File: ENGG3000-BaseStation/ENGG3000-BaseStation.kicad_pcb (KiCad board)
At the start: 4 copper layers, 29 parts, among them J1 Board Power, J2 OLED, J4 USB_C_Receptacle_USB2.0_16P, Q1 SS8050, SW1 RESET, SW2 BOOT, U1 ESP32-S3-WROOM-1-N16R8, U5 AMS1117-3.3

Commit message: Schematic update
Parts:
- removed U5: AMS1117-3.3, Package_TO_SOT_SMD:SOT-223-3_TabPin2
- removed UART0: UART0, Connector_JST:JST_XH_B4B-XH-A_1x04_P2.50mm_Vertical
- added C5: 100nF, Capacitor_SMD:C_0402_1005Metric, F.Cu at (148.8, 74.9)
- added C6: 10uF, Capacitor_Tantalum_SMD:CP_EIA-3216-18_Kemet-A, F.Cu at (149.1, 79.8)
- added C7: 10uF, Capacitor_Tantalum_SMD:CP_EIA-3216-18_Kemet-A, F.Cu at (149.1, 82.9)
- added C8: 1uF, Capacitor_SMD:C_0402_1005Metric, F.Cu at (148.8, 76.8)
- added D4: 5V, LED_SMD:LED_0603_1608Metric, F.Cu at (149.1, 101.7)
- added D5: 3.3V, LED_SMD:LED_0805_2012Metric, F.Cu at (118.7, 102.3)
- added D6: STATUS, LED_SMD:LED_0805_2012Metric, F.Cu at (118.7, 105.3)
- added J3: Cell 1, Connector_JST:JST_XH_B2B-XH-A_1x02_P2.50mm_Vertical, F.Cu at (115.0, 85.0)
- added J5: OLED, Connector_PinHeader_2.54mm:PinHeader_1x04_P2.54mm_Vertical, F.Cu at (123.2, 68.3)
- added J6: Buttons, Connector_PinHeader_2.54mm:PinHeader_1x05_P2.54mm_Vertical, F.Cu at (144.8, 90.6)
- added J7: USB_C_Receptacle_USB2.0_16P, Connector_USB:USB_C_Receptacle_G-Switch_GT-USB-7010ASV, F.Cu at (140.3, 83.6)
- added J8: UltrasonicA, Connector_PinHeader_2.54mm:PinHeader_1x04_P2.54mm_Vertical, F.Cu at (127.8, 68.3)
- added J9: UltrasonicB, Connector_PinHeader_2.54mm:PinHeader_1x04_P2.54mm_Vertical, F.Cu at (132.4, 68.3)
- added L1: 2.2uH, Inductor_SMD:L_APV_ANR4020, F.Cu at (137.3, 103.8)
- added Q2: SS8050, Package_TO_SOT_SMD:SOT-23, F.Cu at (114.0, 104.4)
- added R13: 10k, Resistor_SMD:R_0402_1005Metric, F.Cu at (128.2, 92.8)
- added R14: 1k, Resistor_SMD:R_0402_1005Metric, F.Cu at (128.2, 94.7)
- added R15: 10k, Resistor_SMD:R_0402_1005Metric, F.Cu at (128.2, 96.7)
- added R16: 22, Resistor_SMD:R_0402_1005Metric, F.Cu at (128.2, 98.7)
- added R17: 100R, Resistor_SMD:R_0402_1005Metric, F.Cu at (128.2, 100.7)
- added R18: 1k, Resistor_SMD:R_0402_1005Metric, F.Cu at (128.2, 102.7)
- added R19: 5.1k, Resistor_SMD:R_0402_1005Metric, F.Cu at (131.1, 92.8)
- added R21: 5.1k, Resistor_SMD:R_0402_1005Metric, F.Cu at (131.1, 96.7)
- added R22: 5.1k, Resistor_SMD:R_0402_1005Metric, F.Cu at (131.1, 98.7)
- added R23: 5.1k, Resistor_SMD:R_0402_1005Metric, F.Cu at (131.1, 100.7)
- added R9: 5.1k, Resistor_SMD:R_0402_1005Metric, F.Cu at (125.3, 96.7)
- added U3: TPS63001DRCR, Package_SON:Texas_DRC0010J_ThermalVias, F.Cu at (149.6, 97.9)
- added UART1: UART0, Connector_PinHeader_2.54mm:PinHeader_1x04_P2.54mm_Vertical, F.Cu at (137.0, 68.3)
- C1: value 10uF -> 1uF
- C2: value 10uF -> 1uF; footprint Capacitor_Tantalum_SMD:CP_EIA-3216-18_Kemet-A -> Capacitor_SMD:C_0402_1005Metric
- C3: value 1uF -> 10uF
- C4: footprint Capacitor_Tantalum_SMD:CP_EIA-3216-18_Kemet-A -> Capacitor_SMD:C_0402_1005Metric
- D1: value 5V -> CHRG; footprint LED_SMD:LED_0603_1608Metric -> LED_SMD:LED_0805_2012Metric
- D2: value 3.3V -> SS14; footprint LED_SMD:LED_0805_2012Metric -> Diode_SMD:D_SMA
- D3: value L -> SS14; footprint LED_SMD:LED_0805_2012Metric -> Diode_SMD:D_SMA
- J1: value Board Power -> CHRG LED; footprint Connector_JST:JST_XH_B3B-XH-A_1x03_P2.50mm_Vertical -> Connector_JST:JST_XH_B2B-XH-A_1x02_P2.50mm_Vertical
- J2: value OLED -> Cell 2; footprint Connector_JST:JST_XH_B4B-XH-A_1x04_P2.50mm_Vertical -> Connector_JST:JST_XH_B2B-XH-A_1x02_P2.50mm_Vertical
- J4: value USB_C_Receptacle_USB2.0_16P -> Power Switch; footprint Connector_USB:USB_C_Receptacle_G-Switch_GT-USB-7010ASV -> Connector_PinHeader_2.54mm:PinHeader_1x02_P2.54mm_Vertical
- Q1: value SS8050 -> AO3401A
- R1: value 5.1k -> 1k
- R12: value 10k -> 22
- R2: value 5.1k -> 1.5k
- R20: value 1k -> 5.1k
- R3: value 22 -> 5.1k
- R4: value 22 -> 51k
- R5: value 5.1k -> 200k
- R6, R7: value 5.1k -> 10k
- U1: value ESP32-S3-WROOM-1-N16R8 -> CN3085; footprint PCM_Espressif:ESP32-S3-WROOM-1 -> JLCPCB_Power_Management_ICs:SOP-8_L4.9-W3.9-P1.27-LS6.0-BL-EP
- moved C1 45.0 mm to (148.8, 67.0)
- moved C3 43.2 mm to (148.8, 70.9)
- moved J1 38.6 mm to (115.0, 69.4)
- moved D1 38.2 mm to (118.7, 99.3)
- moved D2 32.3 mm to (143.4, 68.3)
- moved D3 30.9 mm to (143.4, 72.8)
- moved R7 30.0 mm to (125.3, 92.8)
- moved R8 30.0 mm to (125.3, 94.7)
- moved R10 29.3 mm to (125.3, 98.7)
- moved R12 29.3 mm to (125.3, 102.7)
- moved R11 29.3 mm to (125.3, 100.7)
- moved R5 29.0 mm to (122.4, 100.7)
- moved R6 29.0 mm to (122.4, 102.7)
- moved SW1 28.4 mm to (138.5, 91.5)
- moved R1 28.2 mm to (122.4, 92.8)
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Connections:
- C1 pad 1: GND -> +5V
- C1 pad 2: +5V -> GND
- C2 pad 1: +3.3V -> Net-(U2-EN)
- C3 pad 1: Net-(U1-EN) -> BAT
- C4 pad 1: +3.3V -> Net-(U1-RC)
- D1 pad 1: GND -> Net-(D1-K)
- D2 pad 1: GND -> Net-(D2-K)
- D2 pad 2: Net-(D2-A) -> BAT
- D3 pad 1: GND -> Net-(D3-K)
- D3 pad 2: Net-(D3-A) -> +5V
- J1 pad 1: GND -> Net-(D1-K)
- J1 pad 2: +3.3V -> Net-(J1-VCC)
- J2 pad 1: GND -> Net-(J2--)
- J2 pad 2: SDA -> BAT
- Q1 pad 1: Net-(Q1-B) -> Net-(Q1-G)
- Q1 pad 2: GND -> Net-(D2-K)
- Q1 pad 3: Net-(BZ1--) -> Net-(D3-K)
- R1 pad 1: GND -> Net-(U1-ISET)
- R1 pad 2: Net-(J4-CC2) -> Net-(R1-Pad2)
- R10 pad 1: Net-(U1-GPIO0/BOOT) -> Net-(U2-GPIO0/BOOT)
- R11 pad 1: SDA -> GND
- R11 pad 2: +3.3V -> Net-(Q1-G)
- R12 pad 1: SCL -> /ESP_D+
- R12 pad 2: +3.3V -> D+
- R2 pad 1: GND -> Net-(R1-Pad2)
- R2 pad 2: Net-(J4-CC1) -> GND
- R20 pad 1: GPIO41 -> GND
- R20 pad 2: Net-(Q1-B) -> Net-(J7-CC2)
- R3 pad 1: /ESP_D+ -> +3.3V
- R3 pad 2: /D+ -> Net-(U2-EN)
- R4 pad 1: /ESP_D- -> +5V
- R4 pad 2: /D- -> Net-(R4-Pad2)
- R5 pad 1: +5V -> Net-(R4-Pad2)
- R5 pad 2: Net-(D1-A) -> Net-(U1-RC)
- R6 pad 1: +3.3V -> BAT
- R6 pad 2: Net-(D2-A) -> FB
- R7 pad 1: GPIO40 -> FB
- R7 pad 2: Net-(D3-A) -> GND
- R8 pad 1: +3.3V -> Net-(J1-VCC)
- R8 pad 2: Net-(U1-EN) -> +5V
- SW1 pad 2: Net-(U1-EN) -> Net-(U2-EN)
- SW2 pad 1: Net-(U1-GPIO0/BOOT) -> Net-(U2-GPIO0/BOOT)
- U1 pad 2: +3.3V -> Net-(U1-ISET)
- U1 pad 3: Net-(U1-EN) -> GND
- U1 pad 4: unconnected-(U1-GPIO4/TOUCH4/ADC1_CH3-Pad4) -> +5V
- U1 pad 5: unconnected-(U1-GPIO5/TOUCH5/ADC1_CH4-Pad5) -> BAT
- U1 pad 6: unconnected-(U1-GPIO6/TOUCH6/ADC1_CH5-Pad6) -> Net-(U1-RC)
- U1 pad 7: unconnected-(U1-GPIO7/TOUCH7/ADC1_CH6-Pad7) -> Net-(D1-K)
- U1 pad 8: unconnected-(U1-GPIO15/U0RTS/ADC2_CH4/XTAL_32K_P-Pad8) -> FB
- U1 pad 9: unconnected-(U1-GPIO16/U0CTS/ADC2_CH5/XTAL_32K_N-Pad9) -> GND

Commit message: Kicad footprint update
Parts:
- removed D6: STATUS, LED_SMD:LED_0805_2012Metric
- removed J6: Buttons, Connector_PinHeader_2.54mm:PinHeader_1x05_P2.54mm_Vertical
- removed R16: 22, Resistor_SMD:R_0402_1005Metric
- added C9: 10uF, Capacitor_SMD:C_0805_2012Metric, F.Cu at (125.2, 70.4)
- added J10: Cell/Pack 1, Connector_JST:JST_XH_B2B-XH-A_1x02_P2.50mm_Vertical, F.Cu at (114.7, 92.6)
- added JP1: SolderJumper, Jumper:SolderJumper-2_P1.3mm_Bridged2Bar_RoundedPad1.0x1.5mm, F.Cu at (122.4, 81.5)
- added JP2: SolderJumper, Jumper:SolderJumper-2_P1.3mm_Bridged2Bar_RoundedPad1.0x1.5mm, F.Cu at (122.4, 89.0)
- added U2: TPS63001DRCR, Package_SON:Texas_DRC0010J_ThermalVias, F.Cu at (132.9, 91.9)
- C2: value 1uF -> 10uF; footprint Capacitor_SMD:C_0402_1005Metric -> Capacitor_Tantalum_SMD:CP_EIA-3216-18_Kemet-A
- C3: footprint Capacitor_SMD:C_0402_1005Metric -> Capacitor_Tantalum_SMD:CP_EIA-3216-18_Kemet-A
- C4: value 10uF -> 1uF
- C5: value 100nF -> 10uF; footprint Capacitor_SMD:C_0402_1005Metric -> Capacitor_SMD:C_0805_2012Metric
- C6: value 10uF -> 100nF; footprint Capacitor_Tantalum_SMD:CP_EIA-3216-18_Kemet-A -> Capacitor_SMD:C_0402_1005Metric
- C7: value 10uF -> 1uF; footprint Capacitor_Tantalum_SMD:CP_EIA-3216-18_Kemet-A -> Capacitor_SMD:C_0402_1005Metric
- C8: value 1uF -> 10uF; footprint Capacitor_SMD:C_0402_1005Metric -> Capacitor_SMD:C_0805_2012Metric
- D1: value CHRG -> 5V; footprint LED_SMD:LED_0805_2012Metric -> LED_SMD:LED_0603_1608Metric
- D2: value SS14 -> 3.3V; footprint Diode_SMD:D_SMA -> LED_SMD:LED_0805_2012Metric
- D3: value SS14 -> STATUS; footprint Diode_SMD:D_SMA -> LED_SMD:LED_0805_2012Metric
- D4: value 5V -> CHRG; footprint LED_SMD:LED_0603_1608Metric -> LED_SMD:LED_0805_2012Metric
- D5: value 3.3V -> SS14; footprint LED_SMD:LED_0805_2012Metric -> Diode_SMD:D_SMA
- J1: value CHRG LED -> OLED; footprint Connector_JST:JST_XH_B2B-XH-A_1x02_P2.50mm_Vertical -> Connector_PinHeader_2.54mm:PinHeader_1x04_P2.54mm_Vertical
- J2: value Cell 2 -> Buttons; footprint Connector_JST:JST_XH_B2B-XH-A_1x02_P2.50mm_Vertical -> Connector_PinHeader_2.54mm:PinHeader_1x05_P2.54mm_Vertical
- J3: value Cell 1 -> UltrasonicA; footprint Connector_JST:JST_XH_B2B-XH-A_1x02_P2.50mm_Vertical -> Connector_PinHeader_2.54mm:PinHeader_1x04_P2.54mm_Vertical
- J4: value Power Switch -> UltrasonicB; footprint Connector_PinHeader_2.54mm:PinHeader_1x02_P2.54mm_Vertical -> Connector_PinHeader_2.54mm:PinHeader_1x04_P2.54mm_Vertical
- J5: value OLED -> USB_C_Receptacle_USB2.0_16P; footprint Connector_PinHeader_2.54mm:PinHeader_1x04_P2.54mm_Vertical -> Connector_USB:USB_C_Receptacle_G-Switch_GT-USB-7010ASV
- J7: value USB_C_Receptacle_USB2.0_16P -> Power Switch; footprint Connector_USB:USB_C_Receptacle_G-Switch_GT-USB-7010ASV -> Connector_PinHeader_2.54mm:PinHeader_1x02_P2.54mm_Vertical
- J8: value UltrasonicA -> Cell 3; footprint Connector_PinHeader_2.54mm:PinHeader_1x04_P2.54mm_Vertical -> Connector_JST:JST_XH_B2B-XH-A_1x02_P2.50mm_Vertical
- J9: value UltrasonicB -> Cell 2; footprint Connector_PinHeader_2.54mm:PinHeader_1x04_P2.54mm_Vertical -> Connector_JST:JST_XH_B2B-XH-A_1x02_P2.50mm_Vertical
- Q1: value AO3401A -> SS8050
- Q2: value SS8050 -> AO3401A
- R1: value 1k -> 5.1k
- R10, R11: value 10k -> 5.1k
- R12: value 22 -> 1k
- R13: value 10k -> 100R
- R14: value 1k -> 51k
- R15: value 10k -> 200k
- R17: value 100R -> 5.1k
- R18: value 1k -> 10k
- R19, R21: value 5.1k -> 1k
- R2: value 1.5k -> 5.1k
- R20, R23: value 5.1k -> 10k; footprint Resistor_SMD:R_0402_1005Metric -> Resistor_SMD:R_0805_2012Metric_Pad1.20x1.40mm_HandSolder
- R22: value 5.1k -> 1.5k
- R4: value 51k -> 5.1k
- R5: value 200k -> 22
- R6: value 10k -> 22
- R8, R9: value 5.1k -> 10k
- U1: value CN3085 -> ESP32-S3-WROOM-1-N16R8; footprint JLCPCB_Power_Management_ICs:SOP-8_L4.9-W3.9-P1.27-LS6.0-BL-EP -> PCM_Espressif:ESP32-S3-WROOM-1
- U3: value TPS63001DRCR -> CN3085; footprint Package_SON:Texas_DRC0010J_ThermalVias -> JLCPCB_Power_Management_ICs:SOP-8_L4.9-W3.9-P1.27-LS6.0-BL-EP
- moved Q1 92.2 mm to (67.9, 179.8)
- moved BZ1 80.4 mm to (92.0, 158.7)
- moved UART1 80.4 mm to (105.1, 142.1)
- moved R12 78.5 mm to (93.4, 174.5)
- moved R9 78.5 mm to (93.4, 168.5)
- moved R8 78.5 mm to (93.4, 166.5)
- moved J1 76.4 mm to (91.4, 142.1)
- moved J4 71.0 mm to (100.5, 142.1)
- moved J2 65.1 mm to (113.5, 142.2)
- moved J3 60.2 mm to (95.9, 142.1)
- moved U1 55.0 mm to (167.4, 77.1)
- moved R7 54.0 mm to (179.1, 87.8)
- moved D4 44.6 mm to (130.4, 61.2)
- moved U3 43.8 mm to (119.3, 66.3), turned to -90 degrees
- moved C1 41.3 mm to (159.5, 106.9)
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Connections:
- C1 pad 1: +5V -> Net-(U1-EN)
- C2 pad 1: Net-(U2-EN) -> +3.3V
- C3 pad 1: BAT -> +3.3V
- C4 pad 1: Net-(U1-RC) -> +3.3V
- C5 pad 1: Net-(U3-EN) -> VIN
- C6 pad 1: +3.3V -> Net-(U2-EN)
- C7 pad 1: +3.3V -> +5V
- C8 pad 1: +3.3V -> BAT
- D1 pad 1: Net-(D1-K) -> GND
- D2 pad 1: Net-(D2-K) -> GND
- D2 pad 2: BAT -> Net-(D2-A)
- D3 pad 1: Net-(D3-K) -> GND
- D3 pad 2: +5V -> Net-(D3-A)
- D4 pad 1: GND -> Net-(D4-K)
- D5 pad 1: GND -> Net-(D5-K)
- D5 pad 2: Net-(D5-A) -> +5V
- J1 pad 1: Net-(D1-K) -> GND
- J1 pad 2: Net-(J1-VCC) -> SDA
- J2 pad 1: Net-(J2--) -> GND
- J2 pad 2: BAT -> GPIO6
- J3 pad 2: Net-(J2--) -> GPIO1
- J4 pad 1: VIN -> GND
- J4 pad 2: Net-(D3-K) -> GPIO4
- J8 pad 1: GND -> Net-(J8--)
- J8 pad 2: GPIO12 -> BAT
- J9 pad 1: GND -> Net-(J10-+)
- J9 pad 2: GPIO27 -> Net-(J8--)
- L1 pad 1: Net-(U3-L2) -> Net-(U2-L2)
- L1 pad 2: Net-(U3-L1) -> Net-(U2-L1)
- Q1 pad 1: Net-(Q1-G) -> Net-(Q1-B)
- Q1 pad 2: Net-(D2-K) -> GND
- Q1 pad 3: Net-(D3-K) -> Net-(BZ1--)
- Q2 pad 1: Net-(Q2-B) -> Net-(Q2-G)
- Q2 pad 2: GND -> Net-(D5-K)
- Q2 pad 3: Net-(BZ1--) -> BAT
- R1 pad 1: Net-(U1-ISET) -> +3.3V
- R1 pad 2: Net-(R1-Pad2) -> Net-(U1-EN)
- R10 pad 1: Net-(U2-GPIO0/BOOT) -> GND
- R10 pad 2: +3.3V -> Net-(J5-CC2)
- R11 pad 2: Net-(Q1-G) -> Net-(J5-CC1)
- R12 pad 1: /ESP_D+ -> GPIO17
- R12 pad 2: D+ -> Net-(Q1-B)
- R13 pad 1: SDA -> Net-(U2-EN)
- R13 pad 2: +3.3V -> VIN
- R14 pad 1: Net-(Q1-G) -> +5V
- R14 pad 2: +5V -> Net-(R14-Pad2)
- R15 pad 1: SCL -> Net-(R14-Pad2)
- R15 pad 2: +3.3V -> Net-(U3-RC)
- R17 pad 1: Net-(U3-EN) -> Net-(D4-A)
- R17 pad 2: VIN -> +5V
- R18 pad 1: unconnected-(R18-Pad1) -> GND
- R18 pad 2: Net-(Q2-B) -> Net-(Q2-G)
- R19 pad 1: +5V -> Net-(U3-ISET)
- R19 pad 2: Net-(D4-A) -> Net-(R19-Pad2)
- R2 pad 1: Net-(R1-Pad2) -> +5V
- R2 pad 2: GND -> Net-(D1-A)
- R20 pad 1: GND -> BAT
- R20 pad 2: Net-(J7-CC2) -> FB
- R21 pad 1: GND -> +5V
- R21 pad 2: Net-(J7-CC1) -> Net-(Q2-G)
- R22 pad 1: +3.3V -> Net-(R19-Pad2)
- R22 pad 2: Net-(D5-A) -> GND
- R23 pad 1: Ass -> FB
- R23 pad 2: Net-(D6-A) -> GND
- R3 pad 2: Net-(U2-EN) -> Net-(D2-A)
- R4 pad 1: +5V -> GPIO14
- R4 pad 2: Net-(R4-Pad2) -> Net-(D3-A)
- R5 pad 1: Net-(R4-Pad2) -> /ESP_D+
- R5 pad 2: Net-(U1-RC) -> D+
- R6 pad 1: BAT -> /ESP_D-
- R6 pad 2: FB -> D-
- R7 pad 1: FB -> Net-(U1-GPIO0/BOOT)
- R7 pad 2: GND -> +3.3V
- R8 pad 1: Net-(J1-VCC) -> SDA
- R8 pad 2: +5V -> +3.3V
- R9 pad 1: Net-(D1-A) -> SCL
- R9 pad 2: +5V -> +3.3V
- SW1 pad 2: Net-(U2-EN) -> Net-(U1-EN)
- SW2 pad 1: Net-(U2-GPIO0/BOOT) -> Net-(U1-GPIO0/BOOT)
- U1 pad 2: Net-(U1-ISET) -> +3.3V
- U1 pad 3: GND -> Net-(U1-EN)
- U1 pad 4: +5V -> GPIO4
- U1 pad 5: BAT -> unconnected-(U1-GPIO5/TOUCH5/ADC1_CH4-Pad5)
- U1 pad 6: Net-(U1-RC) -> GPIO6
- U1 pad 7: Net-(D1-K) -> GPIO7
- U1 pad 8: FB -> unconnected-(U1-GPIO15/U0RTS/ADC2_CH4/XTAL_32K_P-Pad8)
- U1 pad 9: GND -> unconnected-(U1-GPIO16/U0CTS/ADC2_CH5/XTAL_32K_N-Pad9)
- U3 pad 1: +3.3V -> GND
- U3 pad 2: Net-(U3-L2) -> Net-(U3-ISET)
- U3 pad 4: Net-(U3-L1) -> +5V
- U3 pad 5: VIN -> BAT
- U3 pad 6: Net-(U3-EN) -> Net-(U3-RC)
- U3 pad 7: Net-(U3-EN) -> Net-(D4-K)
- U3 pad 8: Net-(U3-EN) -> FB
- UART1 pad 2: Net-(U2-U0TXD/GPIO43/CLK_OUT1) -> Net-(U1-U0TXD/GPIO43/CLK_OUT1)
- UART1 pad 3: Net-(U2-U0RXD/GPIO44/CLK_OUT2) -> Net-(U1-U0RXD/GPIO44/CLK_OUT2)
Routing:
- net +3.3V: track 0.00 -> 103.7 mm, vias 0 -> 8
- net +5V: track 0.00 -> 70.2 mm, vias 0 -> 5
- net BAT: track 0.00 -> 35.7 mm, vias 0 -> 2
- net D+: track 0.00 -> 29.6 mm
- net D-: track 0.00 -> 28.9 mm
- net Net-(J8--): track 0.00 -> 21.8 mm
- net VIN: track 0.00 -> 16.9 mm, vias 0 -> 2
- net Net-(U1-EN): track 0.00 -> 16.6 mm
- net Net-(J10-+): track 0.00 -> 15.2 mm
- net Net-(D5-K): track 0.00 -> 13.6 mm
- net Net-(U1-GPIO0/BOOT): track 0.00 -> 12.7 mm
- net Net-(D4-K): track 0.00 -> 11.1 mm
- net Net-(U3-RC): track 0.00 -> 7.92 mm
- net GND: track 0.00 -> 7.29 mm
- net Net-(U2-EN): track 0.00 -> 5.58 mm
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- added copper zone on B.Cu, net GND
- added copper zone on F.Cu, net GND
- added copper zone on In1.Cu, net GND
- added copper zone on In2.Cu, net GND
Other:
- board outline added: 80 x 50 mm

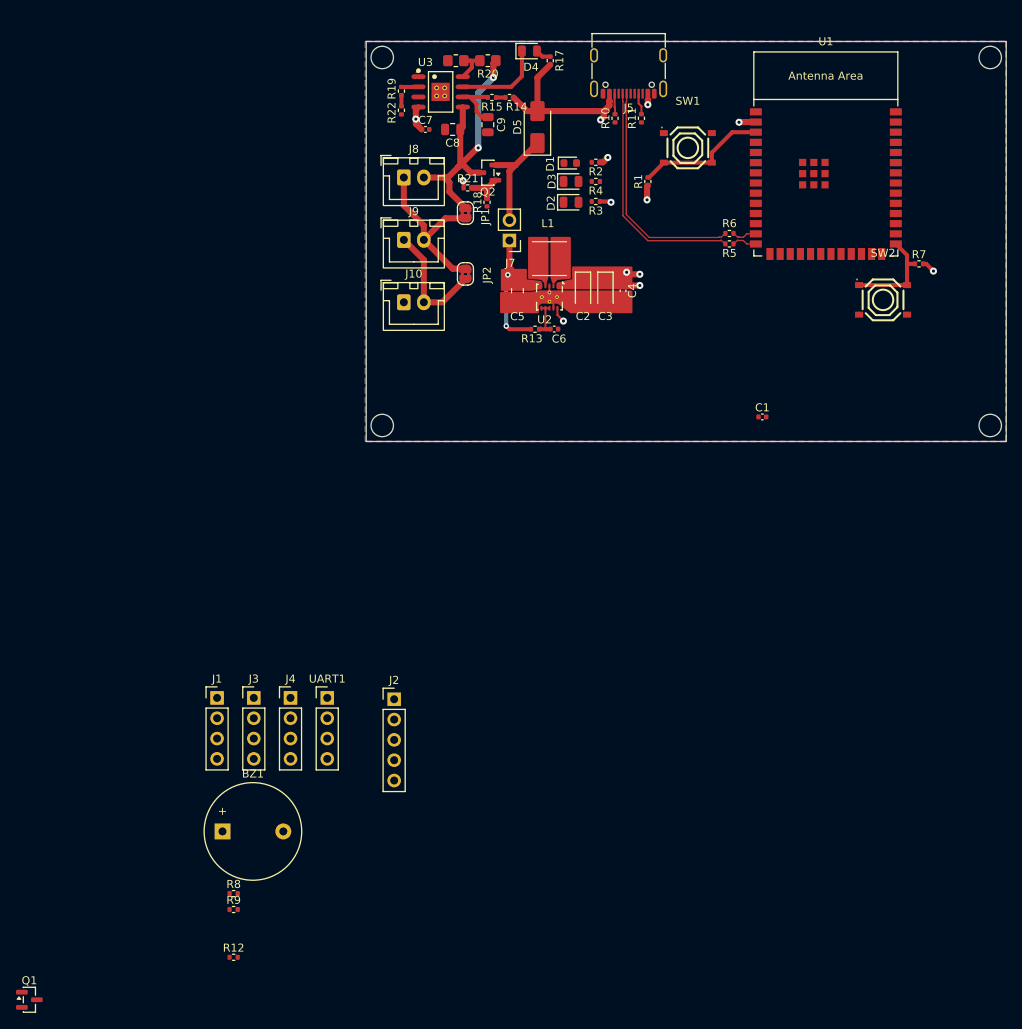
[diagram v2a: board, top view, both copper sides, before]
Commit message: PCB footprint addition and Calibration graphs added
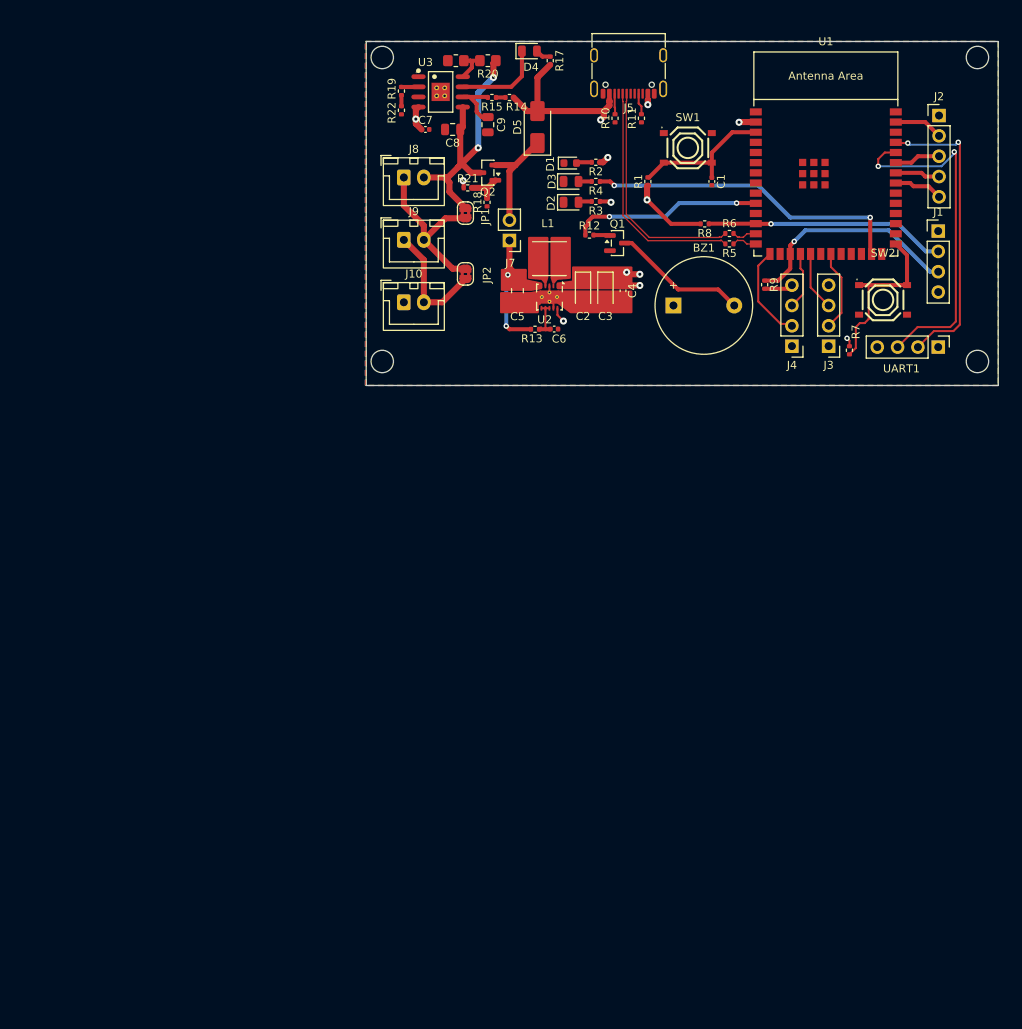
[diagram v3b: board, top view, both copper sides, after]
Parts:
- moved Q1 119.8 mm to (141.4, 85.2)
- moved J1 107.4 mm to (181.5, 83.7)
- moved R9 102.5 mm to (159.8, 90.4), turned to -90 degrees
- moved R8 102.4 mm to (152.3, 82.8), turned to 180 degrees
- moved R12 100.6 mm to (137.9, 84.2)
- moved J2 99.8 mm to (181.6, 69.3)
- moved UART1 88.1 mm to (181.5, 98.2), turned to -90 degrees
- moved BZ1 86.6 mm to (148.4, 93.0)
- moved J3 84.2 mm to (167.8, 98.1), turned to 180 degrees
- moved J4 76.6 mm to (163.2, 98.1), turned to 180 degrees
- moved C1 30.1 mm to (153.2, 77.5), turned to -90 degrees
- moved R7 13.9 mm to (170.4, 98.6), turned to 90 degrees
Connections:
- BZ1 pad 1: +5V -> +3.3V
- J2 pad 2: GPIO6 -> GPIO1
- J2 pad 3: GPIO7 -> GPIO43
- J2 pad 4: GPIO10 -> GPIO41
- J2 pad 5: GPIO11 -> GPIO40
- J3 pad 2: GPIO1 -> GPIO13
- J3 pad 3: GPIO3 -> GPIO11
- J4 pad 2: GPIO4 -> GPIO3
- J4 pad 3: GPIO13 -> GPIO10
- R4 pad 1: GPIO14 -> GPIO48
- U1 pad 22: GPIO14 -> unconnected-(U1-GPIO14/TOUCH14/ADC2_CH3/FSPIWP/FSPIDQS/SUBSPIWP-Pad22)
- U1 pad 25: unconnected-(U1-GPIO48/SPICLK_N/SUBSPICLK_N_DIFF-Pad25) -> GPIO48
- U1 pad 33: unconnected-(U1-MTDO/GPIO40/CLK_OUT2-Pad33) -> GPIO40
- U1 pad 34: unconnected-(U1-MTDI/GPIO41/CLK_OUT1-Pad34) -> GPIO41
- U1 pad 35: unconnected-(U1-MTMS/GPIO42-Pad35) -> GPIO43
- U1 pad 4: GPIO4 -> unconnected-(U1-GPIO4/TOUCH4/ADC1_CH3-Pad4)
- U1 pad 6: GPIO6 -> unconnected-(U1-GPIO6/TOUCH6/ADC1_CH5-Pad6)
- U1 pad 7: GPIO7 -> unconnected-(U1-GPIO7/TOUCH7/ADC1_CH6-Pad7)
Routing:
- net Net-(U1-U0RXD/GPIO44/CLK_OUT2): track 0.00 -> 43.7 mm, vias 0 -> 2
- net GPIO48: track 0.00 -> 40.3 mm, vias 0 -> 2
- net Net-(U1-U0TXD/GPIO43/CLK_OUT1): track 0.00 -> 37.3 mm, vias 0 -> 2
- net +3.3V: track 103.7 -> 138.3 mm
- net SDA: track 0.00 -> 30.1 mm, vias 0 -> 1
- net SCL: track 0.00 -> 28.1 mm, vias 0 -> 1
- net GPIO17: track 0.00 -> 23.8 mm, vias 0 -> 2
- net Net-(BZ1--): track 0.00 -> 16.9 mm
- net GPIO3: track 0.00 -> 12.0 mm
- net GPIO13: track 0.00 -> 10.2 mm
- net Net-(U1-GPIO0/BOOT): track 12.7 -> 21.7 mm
- net GPIO11: track 0.00 -> 7.37 mm
- net GPIO10: track 0.00 -> 7.15 mm
- net GPIO1: track 0.00 -> 6.12 mm
- net GPIO40: track 0.00 -> 6.12 mm
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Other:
- board size 80 x 50 mm -> 79 x 43 mm

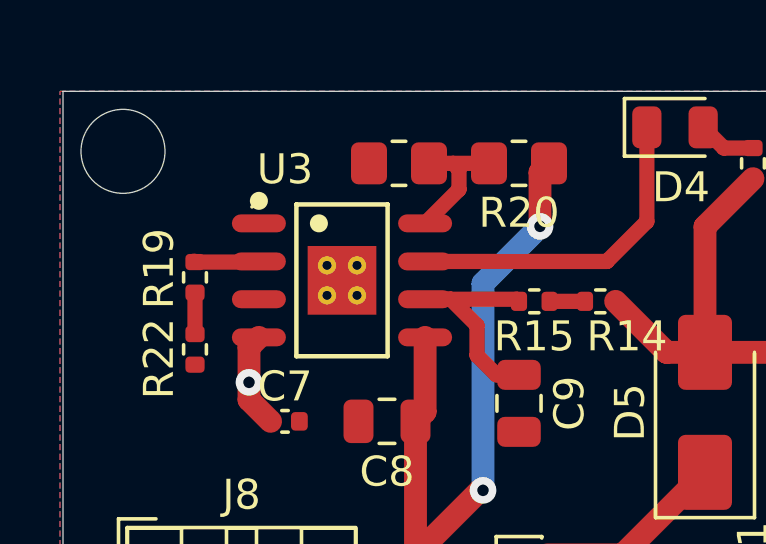
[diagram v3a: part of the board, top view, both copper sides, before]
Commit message: PCB footprint edits
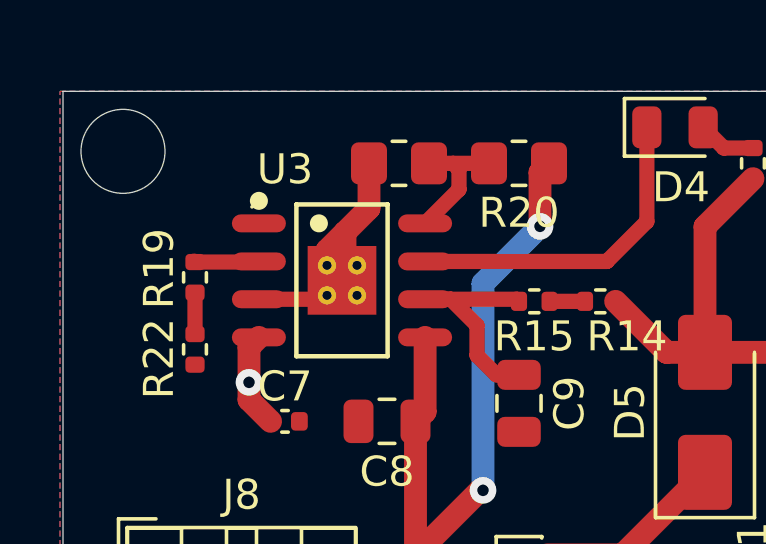
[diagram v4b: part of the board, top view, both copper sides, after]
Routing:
- net GND: track 7.29 -> 16.6 mm
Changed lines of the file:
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@@
 			(unit
 				(name "A")
-				(pins "3" "8" "9" "32" "33" "34" "35" "28" "29" "30" "2" "41" "1" "40"
+				(pins "3" "8" "9" "32" "33" "34" "35" "28" "29" "30" "2" "1" "41" "40"
 					"37" "36" "14" "13" "27" "39" "38" "15" "4" "5" "6" "7" "12" "17" "18"
 					"19" "20" "21" "22" "10" "11" "23" "31" "26" "16" "24" "25"
@@
 	)
 	(segment
+		(start 119.4 65.4)
+		(end 119.8 65.8)
+		(width 0.762)
+		(layer "F.Cu")
+		(net "GND")
+	)
+	(segment
+		(start 119.4 64.7)
+		(end 119.4 65.4)
+		(width 0.762)
+		(layer "F.Cu")
+		(net "GND")
+	)
+	(segment
+		(start 118.8 65.8)
+		(end 118.8 65.3)
+		(width 0.762)
+		(layer "F.Cu")
+		(net "GND")
+	)
+	(segment
 		(start 132.9 90.5475)
 		(end 132.9 91.9475)
@@
 	)
 	(segment
+		(start 120.2 63.9)
+		(end 120.2 62.4)
+		(width 0.762)
+		(layer "F.Cu")
+		(net "GND")
+	)
+	(segment
+		(start 118.8 65.3)
+		(end 119.4 64.7)
+		(width 0.762)
+		(layer "F.Cu")
+		(net "GND")
+	)
+	(segment
 		(start 133.4 93.3475)
 		(end 133.4 92.4475)
@@
 	)
 	(segment
+		(start 119.4 64.7)
+		(end 120.2 63.9)
+		(width 0.762)
+		(layer "F.Cu")
+		(net "GND")
+	)
+	(segment
 		(start 119.3 66.3)
 		(end 119.285075 66.314925)
@@
 	)
 	(segment
+		(start 118.8 66.8)
+		(end 119.8 66.8)
+		(width 0.762)
+		(layer "F.Cu")
+		(net "GND")
+	)
+	(segment
 		(start 133.275 92.5225)
 		(end 133.85 91.9475)
@@
 		(layer "F.Cu")
 		(net "GND")
+	)
+	(segment
+		(start 119.3 66.3)
+		(end 118.67 66.93)
+		(width 0.508)
+		(layer "F.Cu")
+		(net "GND")
+	)
+	(segment
+		(start 118.67 66.93)
+		(end 116.53 66.93)
+		(width 0.508)
+		(layer "F.Cu")
+		(net "GND")
